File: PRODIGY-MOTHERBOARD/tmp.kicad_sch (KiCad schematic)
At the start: 1 part, among them U10 HDC1080

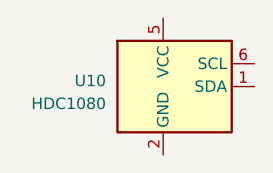
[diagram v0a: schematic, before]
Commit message: project restructure done. Hierarchical sheet done. Outputs/breakouts sheet done
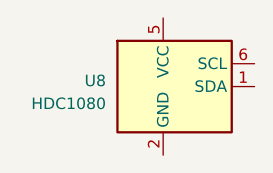
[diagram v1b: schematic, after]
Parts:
- renumbered U10 to U8
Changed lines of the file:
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@@
-(kicad_sch (version 20230121) (generator eeschema)
-  (paper "A4")
-  (symbol (lib_id "Sensor_Humidity:HDC1080") (at 127 72.39 0) (unit 1)
-    (in_bom yes) (on_board yes) (dnp no) (fields_autoplaced)
-    (property "Reference" "U10" (at 118.11 71.755 0)
-      (effects (font (size 1.27 1.27)) (justify right))
-    )
-    (property "Value" "HDC1080" (at 118.11 74.295 0)
-      (effects (font (size 1.27 1.27)) (justify right))
-    )
-    (property "Footprint" "Package_SON:Texas_PWSON-N6" (at 125.73 78.74 0)
-      (effects (font (size 1.27 1.27)) (justify left) hide)
-    )
-    (property "Datasheet" "http://www.ti.com/lit/ds/symlink/hdc1080.pdf" (at 116.84 66.04 0)
-      (effects (font (size 1.27 1.27)) hide)
-    )
-    (pin "1")
-    (pin "2")
-    (pin "3")
-    (pin "4")
-    (pin "5")
-    (pin "6")
-    (pin "7")
-    (instances
-      (project "PRODIGY-MOTHERBOARD"
-        (path "/f1c25860-8989-4190-bd24-2491d23ca7d9/b6067c5b-b0b3-4965-98dd-754256cc3fcc"
-          (reference "U10") (unit 1)
-        )
-      )
-    )
-  )
+(kicad_sch
+	(version 20231120)
+	(generator "eeschema")
+	(generator_version "8.0")
+	(paper "A4")
+	(symbol
+		(lib_id "Sensor_Humidity:HDC1080")
+		(at 127 72.39 0)
+		(unit 1)
+		(exclude_from_sim no)
+		(in_bom yes)
+		(on_board yes)
+		(dnp no)
+		(fields_autoplaced yes)
+		(property "Reference" "U8"
+			(at 118.11 71.755 0)
+			(effects
+				(font
+					(size 1.27 1.27)
+				)
+				(justify right)
+			)
+		)
+		(property "Value" "HDC1080"
+			(at 118.11 74.295 0)
+			(effects
+				(font
+					(size 1.27 1.27)
+				)
+				(justify right)
+			)
+		)
+		(property "Footprint" "Package_SON:Texas_PWSON-N6"
+			(at 125.73 78.74 0)
+			(effects
+				(font
+					(size 1.27 1.27)
+				)
+				(justify left)
+				(hide yes)
+			)
+		)
+		(property "Datasheet" "http://www.ti.com/lit/ds/symlink/hdc1080.pdf"
+			(at 116.84 66.04 0)
+			(effects
+				(font
+					(size 1.27 1.27)
+				)
+				(hide yes)
+			)
+		)
+		(property "Description" ""
+			(at 127 72.39 0)
+			(effects
+				(font
+					(size 1.27 1.27)
+				)
+				(hide yes)
+			)
+		)
+		(pin "1"
+		)
+		(pin "2"
+		)
+		(pin "3"
+		)
+		(pin "4"
+		)
+		(pin "5"
+		)
+		(pin "6"
+		)
+		(pin "7"
+		)
+		(instances
+			(project "PRODIGY-MOTHERBOARD"
+				(path "/f1c25860-8989-4190-bd24-2491d23ca7d9/68745e9f-546d-4e12-ac2b-ba23aeab0093/904942d0-033a-428c-a503-5db171e4e28f"
+					(reference "U8")
+					(unit 1)
+				)
+			)
+		)
+	)
 )
